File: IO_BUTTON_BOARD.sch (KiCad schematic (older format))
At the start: 129 parts, among them P1 I2C, P10 IO_7, P2 I2C, P3 IO_0, P4 IO_1, P5 IO_2, P6 IO_3, P7 IO_4, P8 IO_5, P9 IO_6, Q1 NPN, Q10 PNP, Q11 PNP, Q12 PNP, Q13 PNP, Q2 PNP, Q3 NPN, Q4 PNP, Q5 NPN, Q6 PNP, Q7 PNP, Q8 PNP, Q9 PNP, SW1 I2C_ADDR, SW2 SW_0, SW3 SW_1, SW4 SW_2, SW5 SW_3, SW6 SW_4, SW7 SW_5, SW8 SW_6, SW9 SW_7, U1 PCF8574A, U2 74HC86, U3 74HC86

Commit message: Change Schematic with full separation of alimentations
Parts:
- removed S1: IN_0, Pin_Headers:Pin_Header_Straight_1x03, symbol Switch2RT
- removed S2: IN_1, Pin_Headers:Pin_Header_Straight_1x03, symbol Switch2RT
- removed S3: IN_2, Pin_Headers:Pin_Header_Straight_1x03, symbol Switch2RT
- removed S4: IN_3, Pin_Headers:Pin_Header_Straight_1x03, symbol Switch2RT
- removed S5: IN_4, Pin_Headers:Pin_Header_Straight_1x03, symbol Switch2RT
- removed S6: IN_5, Pin_Headers:Pin_Header_Straight_1x03, symbol Switch2RT
- removed S7: IN_6, Pin_Headers:Pin_Header_Straight_1x03, symbol Switch2RT
- removed S8: IN_7, Pin_Headers:Pin_Header_Straight_1x03, symbol Switch2RT
- removed SW1: I2C_ADDR, Housings_DIP:DIP-8_W7.62mm, symbol SWITCH_x_4
- removed SW2: SW_0, Buttons_Switches_SMD:SW_SPST_EVQPE1, symbol SW_PUSH_SMALL
- removed SW3: SW_1, Buttons_Switches_SMD:SW_SPST_EVQPE1, symbol SW_PUSH_SMALL
- removed SW4: SW_2, Buttons_Switches_SMD:SW_SPST_EVQPE1, symbol SW_PUSH_SMALL
- removed SW5: SW_3, Buttons_Switches_SMD:SW_SPST_EVQPE1, symbol SW_PUSH_SMALL
- removed SW6: SW_4, Buttons_Switches_SMD:SW_SPST_EVQPE1, symbol SW_PUSH_SMALL
- removed SW7: SW_5, Buttons_Switches_SMD:SW_SPST_EVQPE1, symbol SW_PUSH_SMALL
- removed SW8: SW_6, Buttons_Switches_SMD:SW_SPST_EVQPE1, symbol SW_PUSH_SMALL
- removed SW9: SW_7, Buttons_Switches_SMD:SW_SPST_EVQPE1, symbol SW_PUSH_SMALL
- added SW1: CONFIG, symbol SW_DIP_x05
- added SW10, SW11, SW12, SW13, SW14, SW15, SW16, SW17: SW_Push, symbol SW_Push
- added SW2: SW_0, symbol SW_SPDT
- added SW3: SW_1, symbol SW_SPDT
- added SW4: SW_2, symbol SW_SPDT
- added SW5: SW_3, symbol SW_SPDT
- added SW6: SW_4, symbol SW_SPDT
- added SW7: SW_5, symbol SW_SPDT
- added SW8: SW_6, symbol SW_SPDT
- added SW9: SW_7, symbol SW_SPDT
- G1: renamed from G?; footprint (none) -> TO_SOT_Packages_SMD:SOT-353
- P1, P10, P2, P3, P4, P5, P6, P7, P8, P9: footprint Pin_Headers:Pin_Header_Straight_1x04 -> Connectors_Molex:Molex_KK-6410-04_04x2.54mm_Straight
- Q9: renamed from Q?; footprint (none) -> TO_SOT_Packages_SMD:SOT-23
- R10, R11, R15, R16, R17, R18: renamed from R?; footprint (none) -> Resistors_SMD:R_0805
- R12: renamed from R?; value 1k -> 10k; footprint (none) -> Resistors_SMD:R_0805
- U2, U3: symbol 74HC86 -> 74HC86-RESCUE-IO_BUTTON_BOARD
- gave numbers to parts that had none: 7
- renumbered D9 to D10, D10 to D11, D11 to D12, D12 to D13, D13 to D14, D14 to D15, D15 to D16, D16 to D17, D17 to D18, D18 to D19, D19 to D20, D3 to D4, D4 to D5, D5 to D6, D6 to D7, D7 to D8, D8 to D9, Q6 to Q11, Q7 to Q12, Q8 to Q13, Q9 to Q14, Q10 to Q15, Q11 to Q16, Q12 to Q17, Q13 to Q18, R8 to R13, R9 to R14, R10 to R19, R11 to R20, R12 to R21, R13 to R22, R14 to R23, R15 to R24, R16 to R25, R17 to R26, R18 to R27, R19 to R28, R20 to R29, R21 to R30, R22 to R31, R23 to R32, R24 to R33, R25 to R34, R26 to R35, R27 to R36, R28 to R37, R29 to R38, R30 to R39, R31 to R40, R32 to R41, R33 to R42, R34 to R43, R35 to R44, R36 to R45, R37 to R46, R38 to R47, R39 to R48, R40 to R49, R41 to R50, R42 to R51, R51 to R52, R52 to R53, R53 to R54, R54 to R55, R55 to R56, R56 to R57, R57 to R58, R58 to R59, R7 to R9
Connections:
- net ACTIVE_OUTPUT: now also SW1.6
- net CONTACT_LANE: now also SW10.2, SW11.2, SW12.2, SW13.2, SW14.2, SW15.2, SW16.2, SW17.2
- net GND: now also SW1.1, SW1.2, SW1.3
- net IN_0: now also SW2.1 (A)
- net IN_1: now also SW3.1 (A)
- net IN_2: now also SW4.1 (A)
- net IN_3: now also SW5.1 (A)
- net IN_4: now also SW6.1 (A)
- net IN_5: now also SW7.1 (A)
- net IN_6: now also SW8.1 (A)
- net IN_7: now also SW9.1 (A)
- net REVERSE_PULL: now also SW1.7
- net VCC: now also SW1.4, SW1.5
- net at U1.1 (A0): now also SW1.10
- net at U1.2 (A1): now also SW1.9
- net at U1.3 (A2): now also SW1.8
- net at R52.1, U2.1 (IN1): now also SW2.2 (B)
- net at R53.1, U2.4 (IN1): now also SW3.2 (B)
- net at R54.1, U2.9 (IN1): now also SW4.2 (B)
- net at R55.1, U2.12 (IN1): now also SW5.2 (B)
- net at R56.1, U3.1 (IN1): now also SW6.2 (B)
- net at R57.1, U3.4 (IN1): now also SW7.2 (B)
- net at R58.1, U3.9 (IN1): now also SW8.2 (B)
- net at R59.1, U3.12 (IN1): now also SW9.2 (B)
- new net: SW10.1, SW2.3 (C)
- new net: SW11.1, SW3.3 (C)
- new net: SW12.1, SW4.3 (C)
- new net: SW13.1, SW5.3 (C)
- new net: SW14.1, SW6.3 (C)
- new net: SW15.1, SW7.3 (C)
- new net: SW16.1, SW8.3 (C)
- new net: SW17.1, SW9.3 (C)
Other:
- moved on the sheet: C1, D1, D2, D4, P1, P2, Q1, Q2, Q3, Q4, Q5, R1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

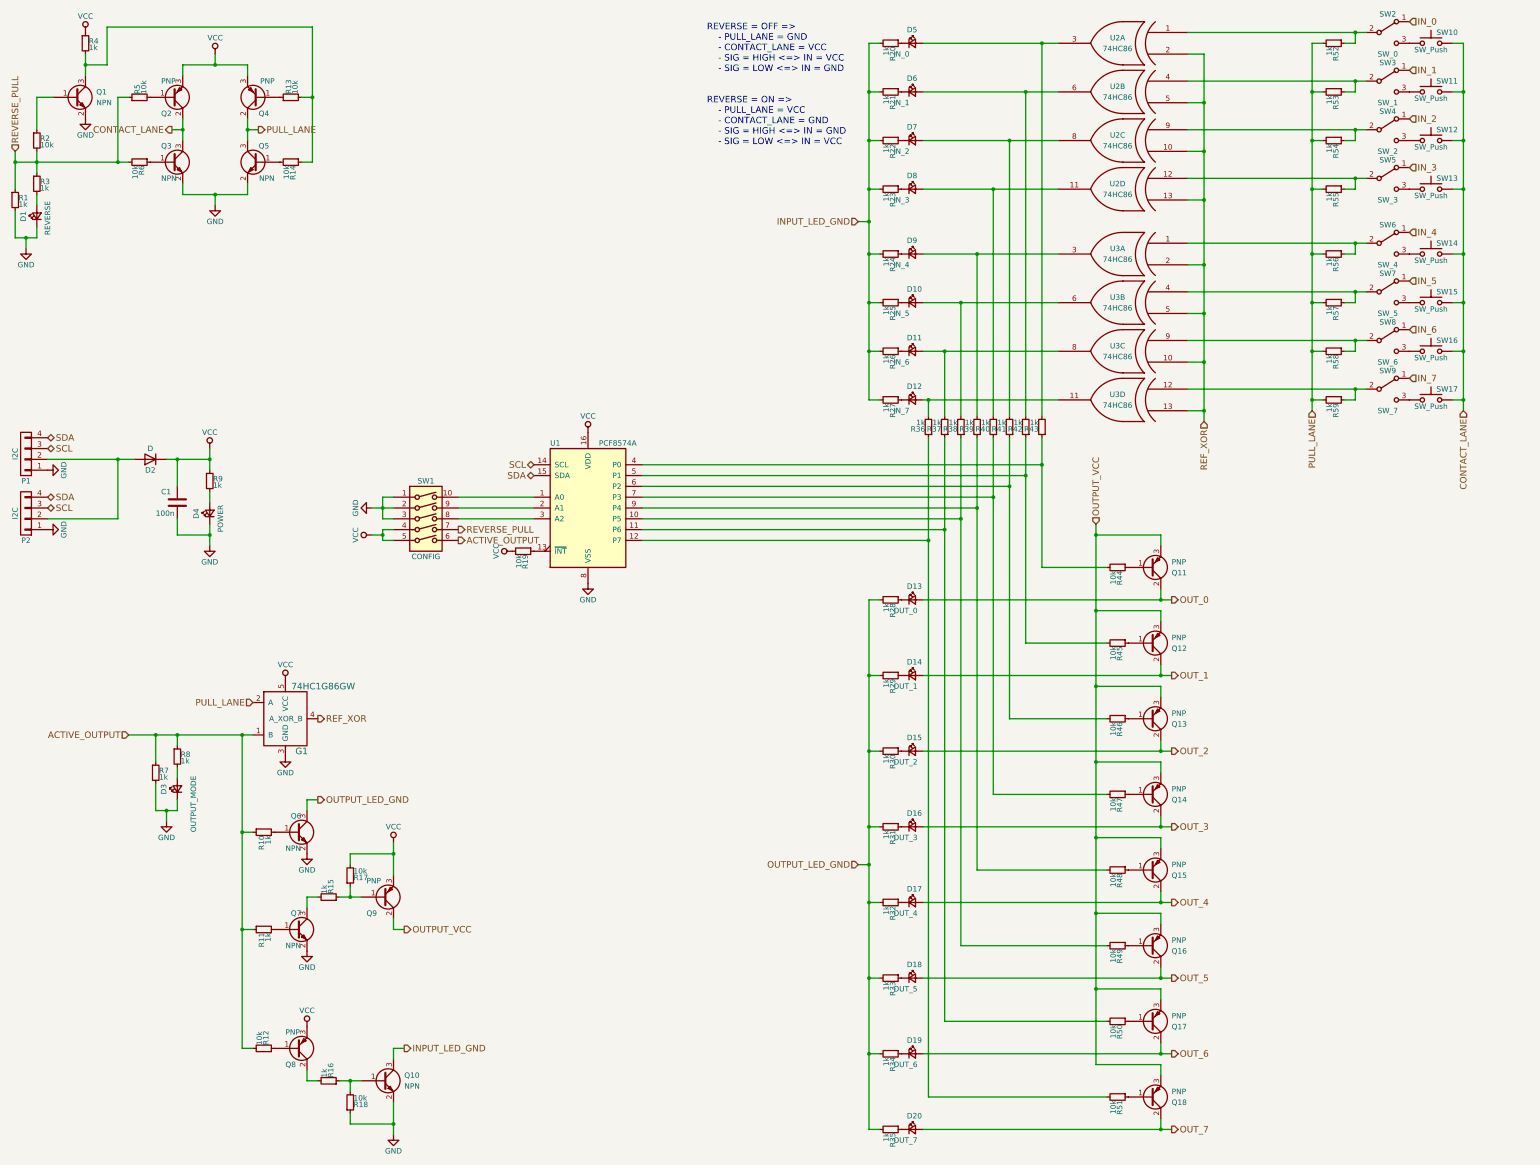
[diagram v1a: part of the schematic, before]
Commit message: Remove alimentation for OUTPUT leds as when the power lane of PNPs is off, leds cannot be turned on
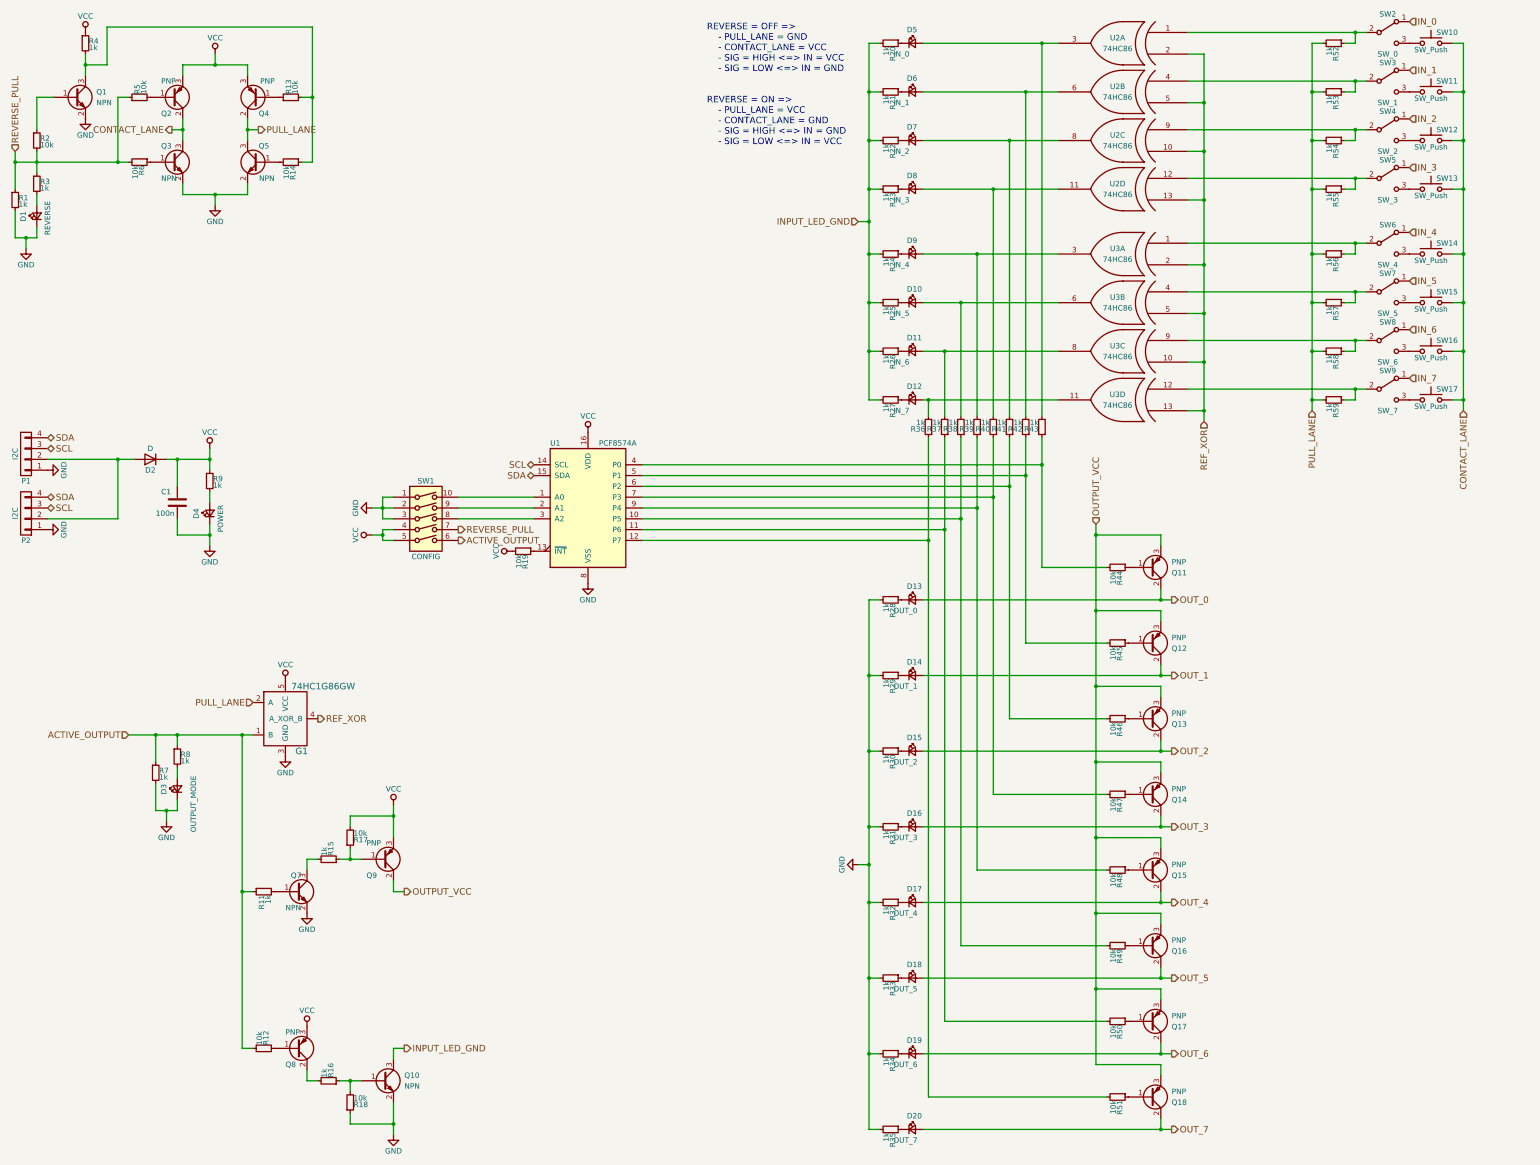
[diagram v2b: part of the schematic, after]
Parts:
- removed Q6: NPN, TO_SOT_Packages_SMD:SOT-23, symbol Q_NPN_BEC
- removed R10: 1k, Resistors_SMD:R_0805, symbol R_Small
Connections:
- net OUTPUT_LED_GND is gone; now on net GND: R28.2, R29.2, R30.2, R31.2, R32.2, R33.2, R34.2, R35.2
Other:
- moved on the sheet: Q7, Q9, R11, R15, R17

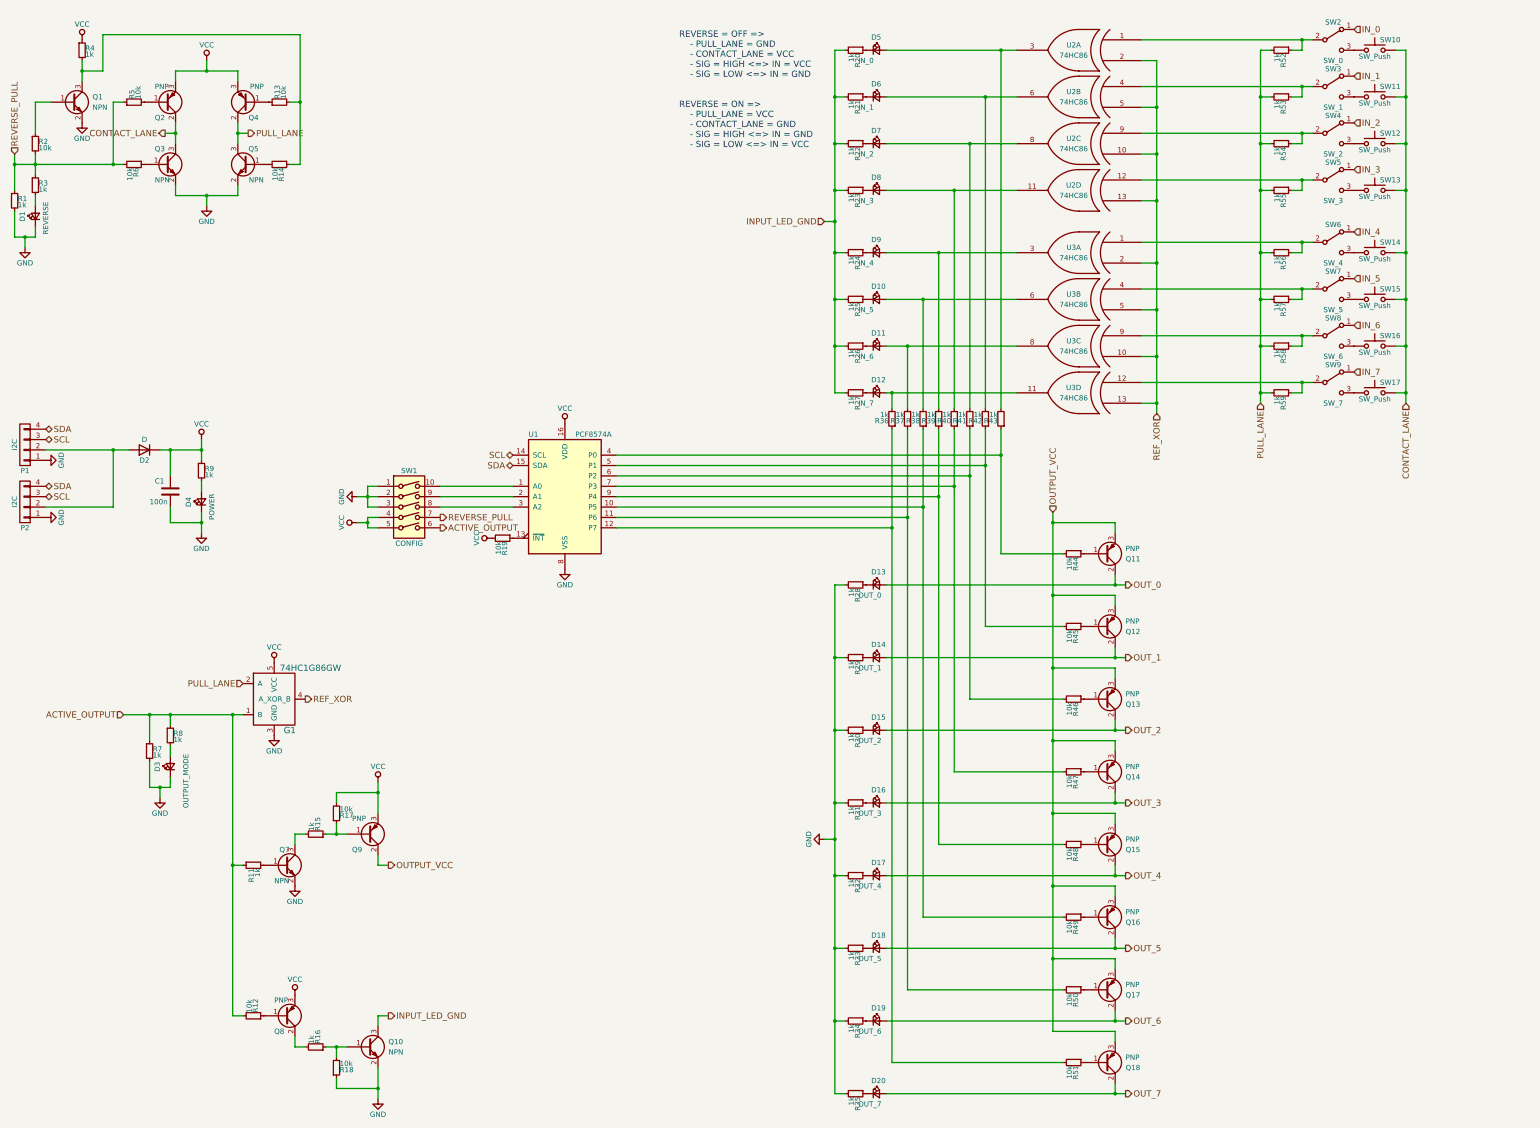
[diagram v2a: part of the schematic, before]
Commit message: Add resistances to protect 74HC86 gates from inputs hazard
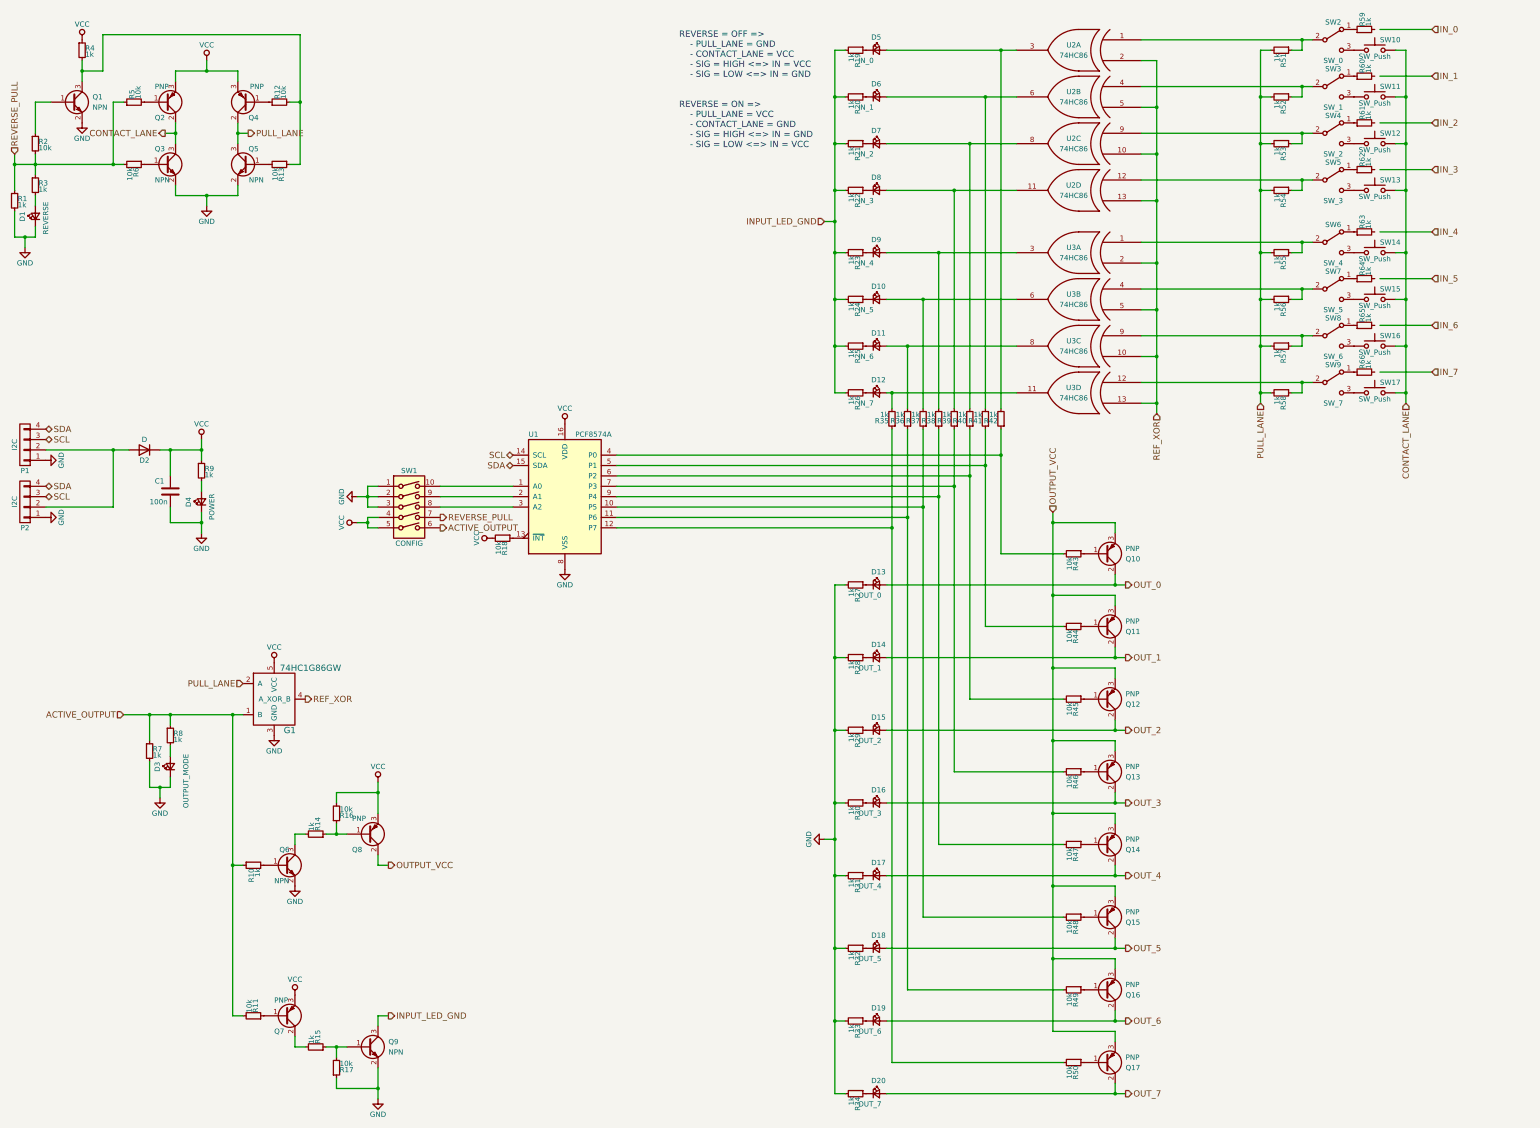
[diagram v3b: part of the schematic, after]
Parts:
- added R59, R60, R61, R62, R63, R64, R65, R66: 1k, Resistors_SMD:R_0805, symbol R_Small
- renumbered Q11 to Q10, Q12 to Q11, Q13 to Q12, Q14 to Q13, Q15 to Q14, Q16 to Q15, Q17 to Q16, Q18 to Q17, Q7 to Q6, Q8 to Q7, Q9 to Q8, Q10 to Q9, R11 to R10, R12 to R11, R13 to R12, R14 to R13, R15 to R14, R16 to R15, R17 to R16, R18 to R17, R19 to R18, R20 to R19, R21 to R20, R22 to R21, R23 to R22, R24 to R23, R25 to R24, R26 to R25, R27 to R26, R28 to R27, R29 to R28, R30 to R29, R31 to R30, R32 to R31, R33 to R32, R34 to R33, R35 to R34, R36 to R35, R37 to R36, R38 to R37, R39 to R38, R40 to R39, R41 to R40, R42 to R41, R43 to R42, R44 to R43, R45 to R44, R46 to R45, R47 to R46, R48 to R47, R49 to R48, R50 to R49, R51 to R50, R52 to R51, R53 to R52, R54 to R53, R55 to R54, R56 to R55, R57 to R56, R58 to R57, R59 to R58
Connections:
- net IN_0: no longer SW2.1 (A)
- net IN_1: no longer SW3.1 (A)
- net IN_2: no longer SW4.1 (A)
- net IN_3: no longer SW5.1 (A)
- net IN_4: no longer SW6.1 (A)
- net IN_5: no longer SW7.1 (A)
- net IN_6: no longer SW8.1 (A)
- net IN_7: no longer SW9.1 (A)
- new net: R64.1, SW7.1 (A)
- new net: R65.1, SW8.1 (A)
- new net: R66.1, SW9.1 (A)
- new net: R63.1, SW6.1 (A)
- new net: R62.1, SW5.1 (A)
- new net: R61.1, SW4.1 (A)
- new net: R59.1, SW2.1 (A)
- new net: R60.1, SW3.1 (A)

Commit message: Add footprints and some RS references
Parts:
- D2: footprint Diodes_SMD:D_0805 -> Diodes_SMD:DO-214AB_Handsoldering; RS (none) -> 688-0512
- SW1: footprint (none) -> Housings_DIP:DIP-10_W7.62mm; RS (none) -> 177-4164
- SW10, SW11, SW12, SW13, SW14, SW15, SW16, SW17: footprint (none) -> Buttons_Switches_SMD:SW_SPST_EVQPE1
- SW2, SW3, SW4, SW5, SW6, SW7, SW8, SW9: footprint (none) -> Pin_Header_1.27:PinSocket_1x03_P1.27mm_Vertical
